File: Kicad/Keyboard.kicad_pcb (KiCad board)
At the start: 2 copper layers, 230.8 x 51.3 mm, 68 parts, among them J1 Power, J2 ext_keys, J3 Keyboard Row, J4 Keyboard Column, J5 Cursor keys, U1 74LS32, U2 74LS32, U3 74LS32, U4 74LS32, U5 74LS32

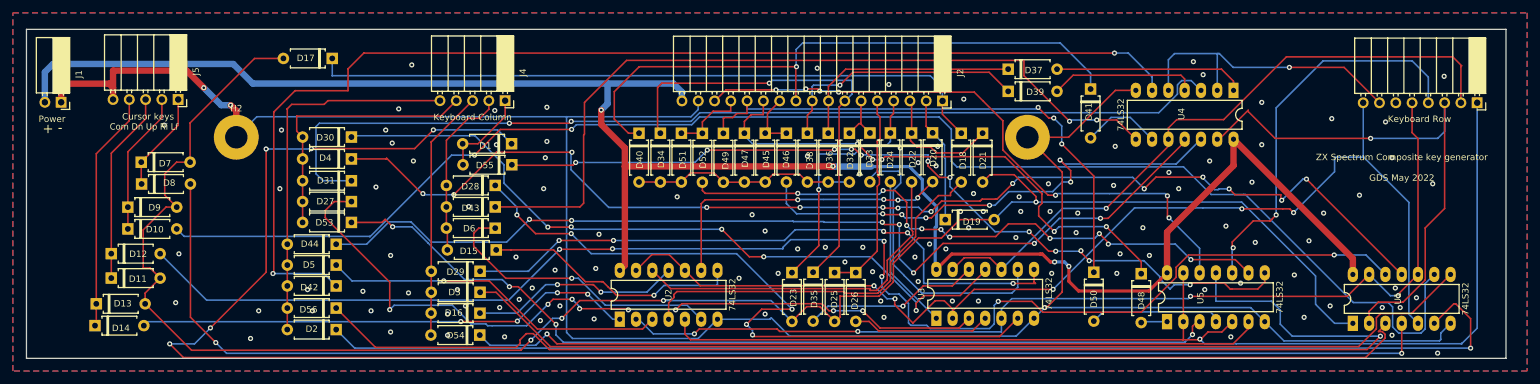
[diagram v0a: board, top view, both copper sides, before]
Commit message: shortened board, correction to link symbol shift to some chars, reversed U4 so it faces the same way as all the other ICs
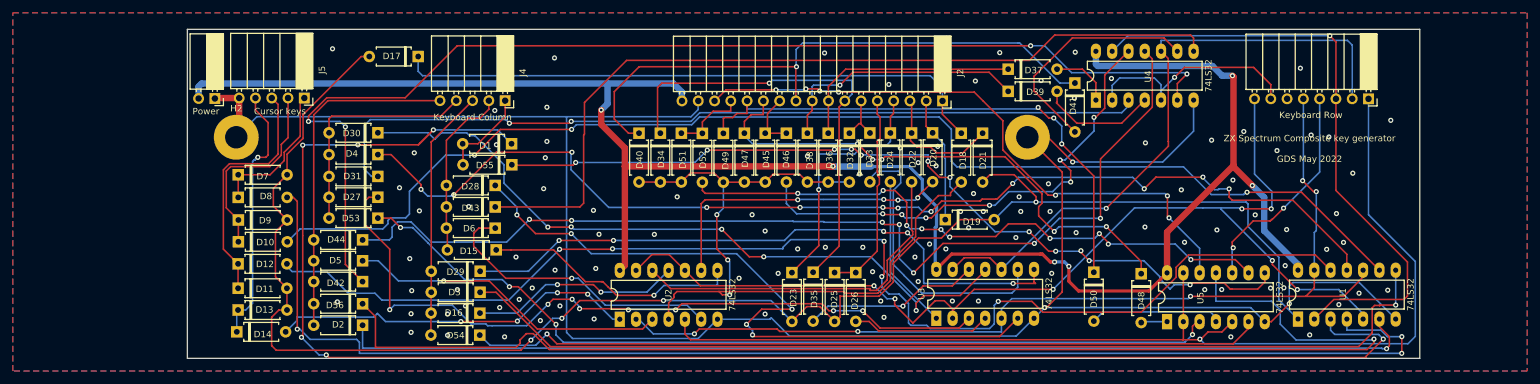
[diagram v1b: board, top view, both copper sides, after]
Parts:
- moved J1 24.0 mm to (62.0, 99.7)
- moved D13 22.1 mm to (65.6, 132.7)
- moved D14 22.1 mm to (65.4, 136.1)
- moved U4 21.5 mm to (199.4, 100.0), turned to 90 degrees
- moved D11 19.8 mm to (65.6, 129.3)
- moved D12 19.8 mm to (65.6, 125.5)
- moved J5 19.7 mm to (76.0, 99.7)
- moved D10 17.4 mm to (65.7, 122.1)
- moved D9 17.4 mm to (65.7, 118.7)
- moved J3 17.0 mm to (241.9, 99.8)
- moved D7 15.3 mm to (65.6, 111.6)
- moved D8 15.2 mm to (65.6, 115.2)
- moved D17 13.4 mm to (93.7, 93.2)
- moved U1 8.58 mm to (230.9, 134.1)
- moved D4 4.18 mm to (87.4, 108.5)
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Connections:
- D32 pad 2: Net-(D32-Pad2) -> Net-(D18-Pad2)
- D34 pad 2: Net-(D32-Pad2) -> Net-(D18-Pad2)
- D36 pad 2: Net-(D32-Pad2) -> Net-(D18-Pad2)
- D38 pad 2: Net-(D32-Pad2) -> Net-(D18-Pad2)
- D40 pad 2: Net-(D32-Pad2) -> Net-(D18-Pad2)
- D45 pad 2: Net-(D32-Pad2) -> Net-(D18-Pad2)
- D47 pad 2: Net-(D32-Pad2) -> Net-(D18-Pad2)
- D49 pad 2: Net-(D32-Pad2) -> Net-(D18-Pad2)
- D51 pad 2: Net-(D32-Pad2) -> Net-(D18-Pad2)
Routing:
- net Net-(D18-Pad2): track 60.2 -> 116.0 mm, vias 0 -> 3
- net Net-(D10-Pad2): track 231.1 -> 193.9 mm, vias 2 -> 3
- net Net-(D32-Pad2): track 35.0 -> 0.00 mm
- net Net-(D12-Pad2): track 220.4 -> 191.3 mm, vias 6 -> 5
- net Net-(D11-Pad2): track 287.1 -> 259.0 mm
- net Net-(J3-Pad4): track 62.1 -> 34.5 mm
- net Net-(D1-Pad1): track 274.5 -> 249.6 mm, vias 5 -> 6
- net Net-(D41-Pad2): track 12.3 -> 37.0 mm
- net Net-(D31-Pad1): track 155.8 -> 131.2 mm
- net GND: track 347.0 -> 325.0 mm, vias 121 -> 109
- net Net-(D2-Pad1): track 190.6 -> 168.8 mm
- net Net-(D14-Pad2): track 78.1 -> 57.7 mm
- net Net-(D37-Pad2): track 29.7 -> 9.66 mm
- net Net-(D17-Pad1): track 107.0 -> 93.4 mm
- net Net-(D4-Pad1): track 188.1 -> 175.0 mm, vias 14 -> 12
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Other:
- board size 230.8 x 51.3 mm -> 192.2 x 51.3 mm
- board text added: "A11 (1-5) A10 (Q-T) A09 (A-G) A12 (6-0) A13 (P=Y) A08 (CS-V) A14 (En-H) A15 (SP-B)"
- board text removed: "A11 (1-5) A10 (Q-T) A09 (A-G) A12 (6-0) A13 (P=Y) A08 (CS-V) A14 (Ent-H) A15 (SPC-B)"
